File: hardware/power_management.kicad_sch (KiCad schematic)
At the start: 5 parts, among them Q1 IRLML6402, U2 BMS Module

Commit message: Added information, footprints and 3d models for several components
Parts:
- D3: Package (none) -> SOD-323F; Part Num (none) -> PMEG4010CEJ,115; Price/unit (none) -> $0.0699; Supplier Link (none) -> https://jlcpcb.com/partdetail/Nexperia-PMEG4010CEJ115/C50704
- Q1: Package (none) -> SOT-23; Part Num (none) -> IRLML6402TRPBF; Price/unit (none) -> $0.0906; Supplier Link (none) -> https://jlcpcb.com/partdetail/InfineonTechnologies-IRLML640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
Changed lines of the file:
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@@
 			)
 		)
-		(property "Datasheet" "https://assets.nexperia.com/documents/data-sheet/PMEG4010CEH_PMEG4010CEJ.pdf"
-			(at 177.8 74.93 0)
-			(effects
-				(font
-					(size 1.27 1.27)
-				)
-				(hide yes)
-			)
-		)
-		(property "Description" "40V, 1A very low Vf MEGA Schottky barrier rectifier, SOD-323F"
+		(property "Datasheet" "https://www.lcsc.com/datasheet/lcsc_datasheet_1809291616_Nexperia-PMEG4010CEJ-115_C50704.pdf"
+			(at 177.8 74.93 0)
+			(effects
+				(font
+					(size 1.27 1.27)
+				)
+				(hide yes)
+			)
+		)
+		(property "Description" "40V 570mV@1A 1A SOD-323F Schottky Diodes ROHS"
+			(at 177.8 74.93 0)
+			(effects
+				(font
+					(size 1.27 1.27)
+				)
+				(hide yes)
+			)
+		)
+		(property "Supplier Link" "https://jlcpcb.com/partdetail/Nexperia-PMEG4010CEJ115/C50704"
+			(at 177.8 74.93 0)
+			(effects
+				(font
+					(size 1.27 1.27)
+				)
+				(hide yes)
+			)
+		)
+		(property "Price/unit" "$0.0699"
+			(at 177.8 74.93 0)
+			(effects
+				(font
+					(size 1.27 1.27)
+				)
+				(hide yes)
+			)
+		)
+		(property "Part Num" "PMEG4010CEJ,115"
+			(at 177.8 74.93 0)
+			(effects
+				(font
+					(size 1.27 1.27)
+				)
+				(hide yes)
+			)
+		)
+		(property "Package" "SOD-323F"
 			(at 177.8 74.93 0)
 			(effects
@@
 			)
 		)
-		(property "Datasheet" "https://www.infineon.com/dgdl/irlml6402pbf.pdf?fileId=5546d462533600a401535668d5c2263c"
+		(property "Datasheet" "https://www.lcsc.com/datasheet/lcsc_datasheet_1810271032_Infineon-Technologies-IRLML6402TRPBF_C2593.pdf"
 			(at 173.99 93.98 0)
 			(effects
@@
 			)
 		)
-		(property "Description" "-3.7A Id, -20V Vds, 65mOhm Rds, P-Channel HEXFET Power MOSFET, SOT-23"
-			(at 170.18 88.9 0)
-			(effects
+		(property "Description" "20V 3.7A 1.3W 65mΩ@4.5V,3.7A 1.2V@250uA 1 Piece P-Channel SOT-23 MOSFETs ROHS"
+			(at 170.18 88.9 0)
+			(effects
+				(font
+					(size 1.27 1.27)
+				)
+				(hide yes)
+			)
+		)
+		(property "Supplier Link" "https://jlcpcb.com/partdetail/InfineonTechnologies-IRLML6402TRPBF/C2593"
+			(at 170.18 88.9 0)
+			(effects
+				(font
+					(size 1.27 1.27)
+				)
+				(hide yes)
+			)
+		)
+		(property "Price/unit" "$0.0906"
+			(at 170.18 88.9 0)
+			(effects
+				(font
+					(size 1.27 1.27)
+				)
+				(hide yes)
+			)
+		)
+		(property "Part Num" "IRLML6402TRPBF"
+			(at 170.18 88.9 0)
+			(effects
+				(font
+					(size 1.27 1.27)
+				)
+				(hide yes)
+			)
+		)
+		(property "Package" "SOT-23"
+			(at 170.18 88.9 0)
+			(effects

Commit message: Added some information to the microcontroller sch and the power_management sch
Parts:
- U2: Package (none) -> Module; Part Num (none) -> TP4056; Price/unit (none) -> 45 kr; Supplier Link (none) -> https://www.electrokit.com/batteriladdare-lipo-microusb
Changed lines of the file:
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@@
 			)
 		)
-		(property "Datasheet" ""
+		(property "Datasheet" "https://dlnmh9ip6v2uc.cloudfront.net/datasheets/Prototyping/TP4056.pdf"
 			(at 113.03 82.55 0)
 			(effects
@@
 			)
 		)
-		(property "Description" ""
+		(property "Description" "TP4056 laddare med skyddskrets för Li-Ion- och LiPo-cell"
 			(at 113.03 82.55 0)
 			(effects
 				(font
+					(size 1.27 1.27)
+				)
+				(hide yes)
+			)
+		)
+		(property "Package" "Module"
+			(at 113.03 81.28 0)
+			(effects
+				(font
+					(size 1.27 1.27)
+				)
+				(hide yes)
+			)
+		)
+		(property "Part Num" "TP4056"
+			(at 113.03 81.28 0)
+			(effects
+				(font
+					(size 1.27 1.27)
+				)
+				(hide yes)
+			)
+		)
+		(property "Price/unit" "45 kr"
+			(at 113.03 81.28 0)
+			(effects
+				(font
+					(size 1.27 1.27)
+				)
+				(hide yes)
+			)
+		)
+		(property "Supplier Link" "https://www.electrokit.com/batteriladdare-lipo-microusb"
+			(at 113.03 81.28 0)
+			(effects
+				(font

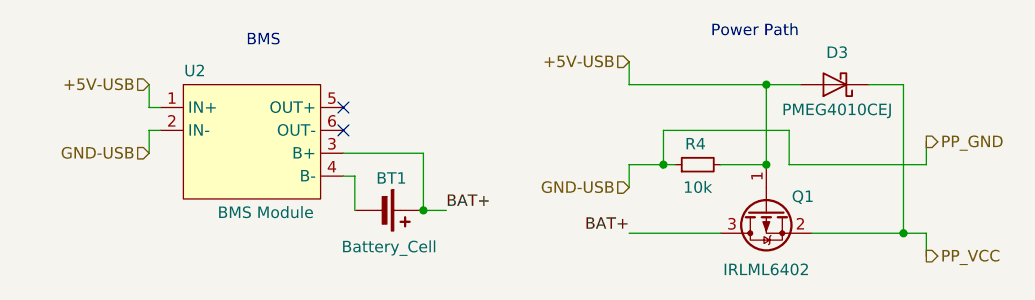
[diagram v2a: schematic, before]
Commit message: Added TP4056 footprint andconfirmed components in UART and BMS schematics.
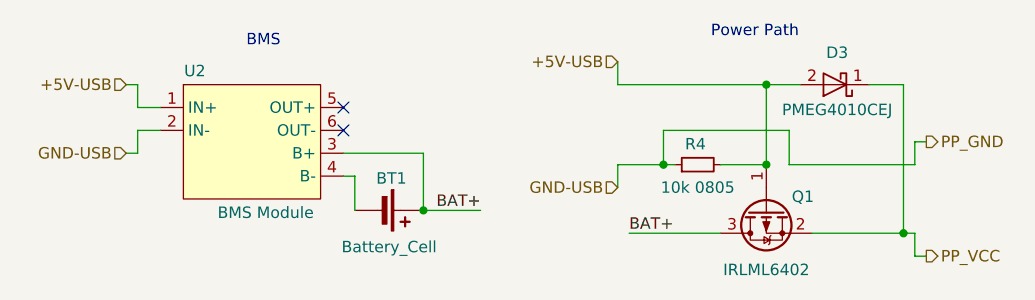
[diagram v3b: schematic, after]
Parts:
- R4: value 10k -> 10k 0805; Package (none) -> 0805; Part Num (none) -> 0805W8F1002T5E; Price/unit (none) -> $0.0017; Supplier Link (none) -> https://jlcpcb.com/partdetail/18102-0805W8F1002T5E/C17414
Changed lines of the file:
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@@
 	(wire
 		(pts
-			(xy 154.94 72.39) (xy 154.94 74.93)
-		)
-		(stroke
-			(width 0)
-			(type default)
-		)
-	)
-	(wire
-		(pts
-			(xy 185.42 91.44) (xy 187.96 91.44)
-		)
-		(stroke
-			(width 0)
-			(type default)
-		)
-	)
-	(wire
-		(pts
-			(xy 154.94 74.93) (xy 170.18 74.93)
+			(xy 186.69 81.28) (xy 187.96 81.28)
+		)
+		(stroke
+			(width 0)
+			(type default)
+		)
+	)
+	(wire
+		(pts
+			(xy 153.67 72.39) (xy 153.67 74.93)
+		)
+		(stroke
+			(width 0)
+			(type default)
+		)
+	)
+	(wire
+		(pts
+			(xy 185.42 91.44) (xy 186.69 91.44)
+		)
+		(stroke
+			(width 0)
+			(type default)
+		)
+	)
+	(wire
+		(pts
+			(xy 153.67 74.93) (xy 170.18 74.93)
 		)
 		(stroke
@@
 	(wire
 		(pts
-			(xy 132.08 88.9) (xy 134.62 88.9)
+			(xy 132.08 88.9) (xy 138.43 88.9)
+		)
+		(stroke
+			(width 0)
+			(type default)
+		)
+	)
+	(wire
+		(pts
+			(xy 100.33 74.93) (xy 100.33 77.47)
 		)
 		(stroke
@@
 	(wire
 		(pts
-			(xy 187.96 91.44) (xy 187.96 93.98)
+			(xy 186.69 91.44) (xy 186.69 93.98)
 		)
 		(stroke
@@
 	(wire
 		(pts
-			(xy 101.6 74.93) (xy 101.6 77.47)
-		)
-		(stroke
-			(width 0)
-			(type default)
-		)
-	)
-	(wire
-		(pts
-			(xy 154.94 83.82) (xy 158.75 83.82)
+			(xy 100.33 82.55) (xy 99.06 82.55)
+		)
+		(stroke
+			(width 0)
+			(type default)
+		)
+	)
+	(wire
+		(pts
+			(xy 153.67 83.82) (xy 158.75 83.82)
 		)
 		(stroke
@@
 	(wire
 		(pts
-			(xy 154.94 83.82) (xy 154.94 86.36)
-		)
-		(stroke
-			(width 0)
-			(type default)
-		)
-	)
-	(wire
-		(pts
-			(xy 101.6 77.47) (xy 102.87 77.47)
+			(xy 153.67 83.82) (xy 153.67 86.36)
+		)
+		(stroke
+			(width 0)
+			(type default)
+		)
+	)
+	(wire
+		(pts
+			(xy 100.33 77.47) (xy 102.87 77.47)
 		)
 		(stroke
@@
 	(wire
 		(pts
-			(xy 187.96 81.28) (xy 187.96 83.82)
+			(xy 186.69 81.28) (xy 186.69 83.82)
 		)
 		(stroke
@@
 	(wire
 		(pts
+			(xy 100.33 74.93) (xy 99.06 74.93)
+		)
+		(stroke
+			(width 0)
+			(type default)
+		)
+	)
+	(wire
+		(pts
 			(xy 123.19 82.55) (xy 132.08 82.55)
 		)
@@
 	(wire
 		(pts
-			(xy 187.96 83.82) (xy 172.72 83.82)
+			(xy 186.69 83.82) (xy 172.72 83.82)
 		)
 		(stroke
@@
 	(wire
 		(pts
+			(xy 100.33 80.01) (xy 100.33 82.55)
+		)
+		(stroke
+			(width 0)
+			(type default)
+		)
+	)
+	(wire
+		(pts
 			(xy 170.18 74.93) (xy 173.99 74.93)
 		)
@@
 	(wire
 		(pts
-			(xy 101.6 80.01) (xy 101.6 82.55)
+			(xy 186.69 93.98) (xy 187.96 93.98)
 		)
 		(stroke
@@
 	(wire
 		(pts
-			(xy 101.6 80.01) (xy 102.87 80.01)
+			(xy 100.33 80.01) (xy 102.87 80.01)
 		)
 		(stroke
@@
 	)
 	(label "BAT+"
-		(at 154.94 91.44 180)
+		(at 154.94 91.44 0)
+		(fields_autoplaced yes)
+		(effects
+			(font
+				(size 1.27 1.27)
+			)
+			(justify left bottom)
+		)
+	)
+	(label "BAT+"
+		(at 138.43 88.9 180)
 		(fields_autoplaced yes)
 		(effects
@@
 			)
 			(justify right bottom)
-		)
-	)
-	(label "BAT+"
-		(at 134.62 88.9 0)
-		(fields_autoplaced yes)
-		(effects
-			(font
-				(size 1.27 1.27)
-			)
-			(justify left bottom)
 		)
 	)
 	(hierarchical_label "GND-USB"
 		(shape input)
-		(at 154.94 86.36 180)
+		(at 153.67 86.36 180)
 		(fields_autoplaced yes)
 		(effects
@@
 	(hierarchical_label "+5V-USB"
 		(shape input)
-		(at 154.94 72.39 180)
+		(at 153.67 72.39 180)
 		(fields_autoplaced yes)
 		(effects
@@
 	(hierarchical_label "+5V-USB"
 		(shape input)
-		(at 101.6 74.93 180)
+		(at 99.06 74.93 180)
 		(fields_autoplaced yes)
 		(effects
@@
 	(hierarchical_label "GND-USB"
 		(shape input)
-		(at 101.6 82.55 180)
+		(at 99.06 82.55 180)
 		(fields_autoplaced yes)
 		(effects
@@
 			)
 		)
-		(property "Value" "10k"
+		(property "Value" "10k 0805"
 			(at 162.56 86.36 90)
 			(effects
@@
 			)
 		)
-		(property "Datasheet" "~"
-			(at 162.56 83.82 0)
-			(effects
-				(font
-					(size 1.27 1.27)
-				)
-				(hide yes)
-			)
-		)
-		(property "Description" "Resistor, small symbol"
-			(at 162.56 83.82 0)
-			(effects
+		(property "Datasheet" "https://jlcpcb.com/api/file/downloadByFileSystemAccessId/8562006748401074176"
+			(at 162.56 83.82 0)
+			(effects
+				(font
+					(size 1.27 1.27)
+				)
+				(hide yes)
+			)
+		)
+		(property "Description" "Resistor"
+			(at 162.56 83.82 0)
+			(effects
+				(font
+					(size 1.27 1.27)
+				)
+				(hide yes)
+			)
+		)
+		(property "Supplier Link" "https://jlcpcb.com/partdetail/18102-0805W8F1002T5E/C17414"
+			(at 162.56 83.82 0)
+			(effects
+				(font
+					(size 1.27 1.27)
+				)
+				(hide yes)
+			)
+		)
+		(property "Price/unit" "$0.0017"
+			(at 162.56 83.82 0)
+			(effects
+				(font
+					(size 1.27 1.27)
+				)
+				(hide yes)
+			)
+		)
+		(property "Part Num" "0805W8F1002T5E"
+			(at 162.56 83.82 0)
+			(effects
+				(font
+					(size 1.27 1.27)
+				)
+				(hide yes)
+			)
+		)
+		(property "Package" "0805"
+			(at 162.56 83.82 0)
+			(effects

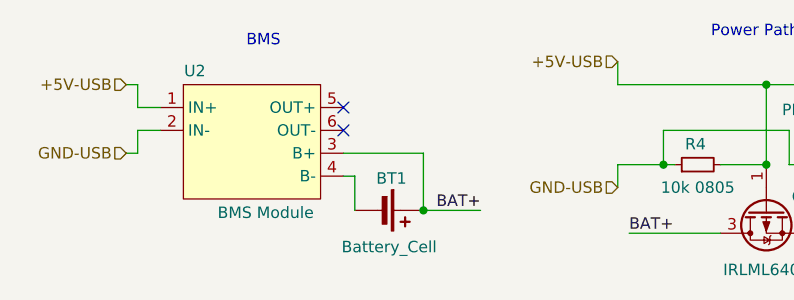
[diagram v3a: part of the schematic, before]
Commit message: Removed the 3.3V Regulator since we might need to run everything out of 5V
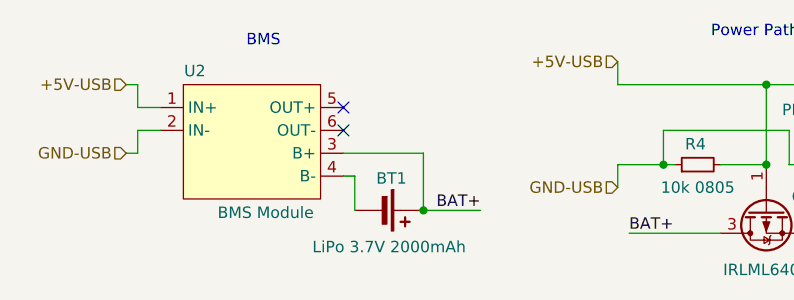
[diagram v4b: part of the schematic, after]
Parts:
- BT1: value Battery_Cell -> LiPo 3.7V 2000mAh
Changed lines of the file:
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@@
 			)
 		)
-		(property "Value" "Battery_Cell"
+		(property "Value" "LiPo 3.7V 2000mAh"
 			(at 128.27 92.964 90)
 			(effects
@@
 			(at 127 88.9 0)
 			(effects
+				(font
+					(size 1.27 1.27)
+				)
+				(hide yes)
+			)
+		)
+		(property "Supplier Link" ""
+			(at 127 88.9 0)
+			(effects
+				(font
+					(size 1.27 1.27)
+				)
+				(hide yes)
+			)
+		)
+		(property "Price/unit" ""
+			(at 127 88.9 0)
+			(effects
+				(font
+					(size 1.27 1.27)
+				)
+				(hide yes)
+			)
+		)
+		(property "Part Num" ""
+			(at 127 88.9 0)
+			(effects
+				(font
+					(size 1.27 1.27)
+				)
+				(hide yes)
+			)
+		)
+		(property "Package" ""
+			(at 127 88.9 0)
+			(effects

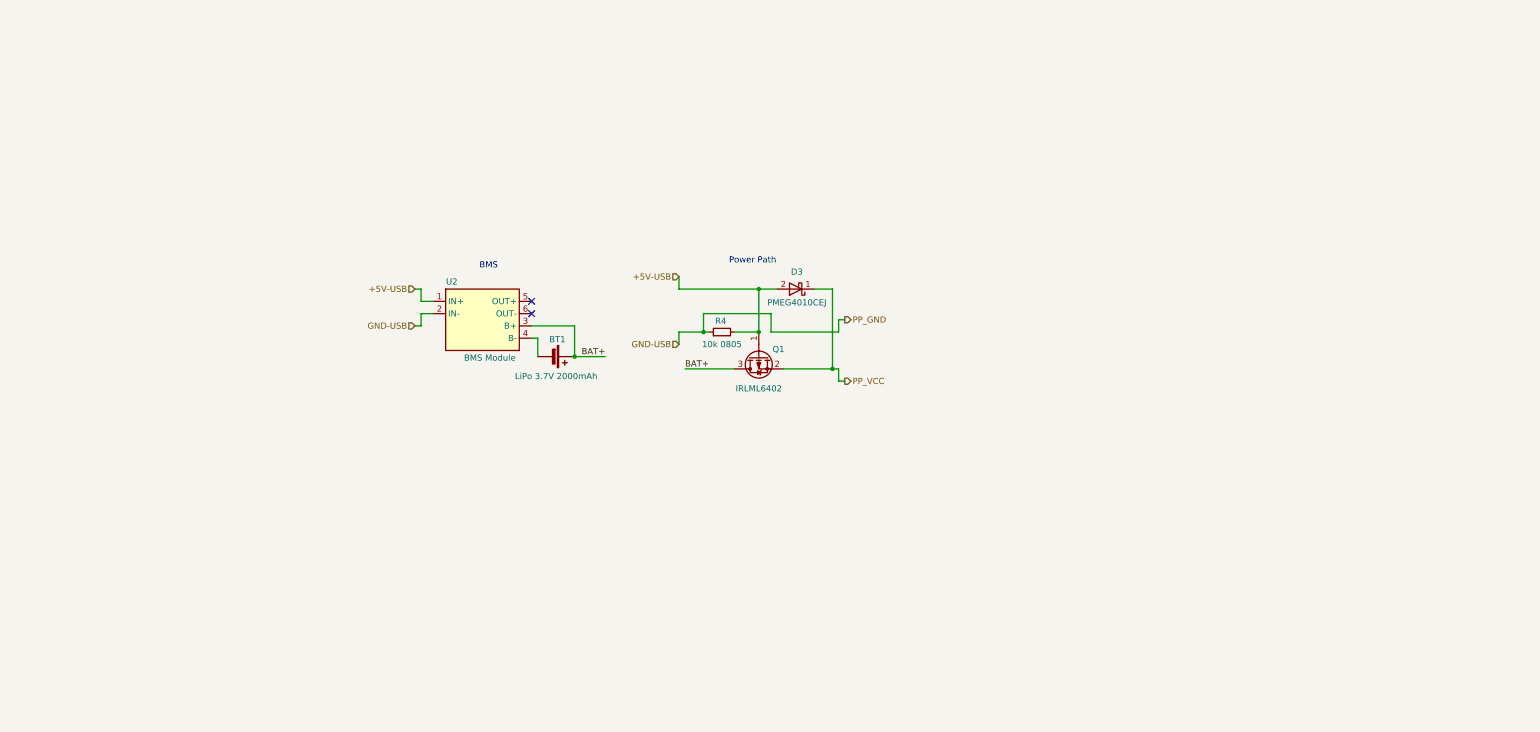
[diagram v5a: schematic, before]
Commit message: Schematic completed, commented and ready for review
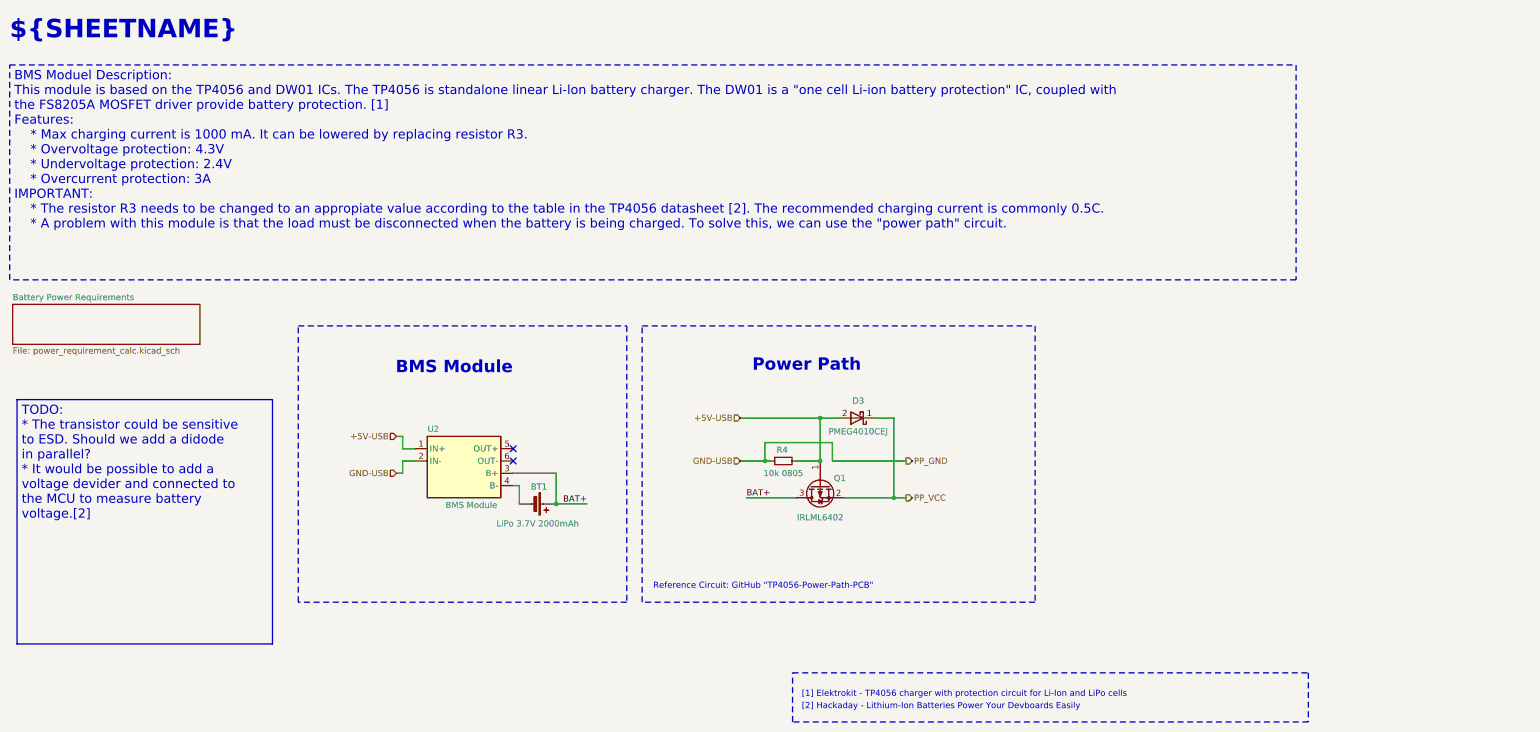
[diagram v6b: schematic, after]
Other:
- added sheet Battery Power Requirements (power_requirement_calc.kicad_sch)
- note added: "${SHEETNAME}"
- note added: "BMS Module"
- note added: "Reference Circuit: GitHub "TP4056-Power-Path-PCB""
- note added: "[1] Elektrokit - TP4056 charger with protection circuit for Li-Ion and LiPo cells"
- note added: "[2] Hackaday - Lithium-Ion Batteries Power Your Devboards Easily"
- note removed: "BMS"
- title: Kitchen_Timer - Power Management -> Kitchen_Timer - ${SHEETNAME}
- moved on the sheet: BT1, D3, Q1, R4, U2

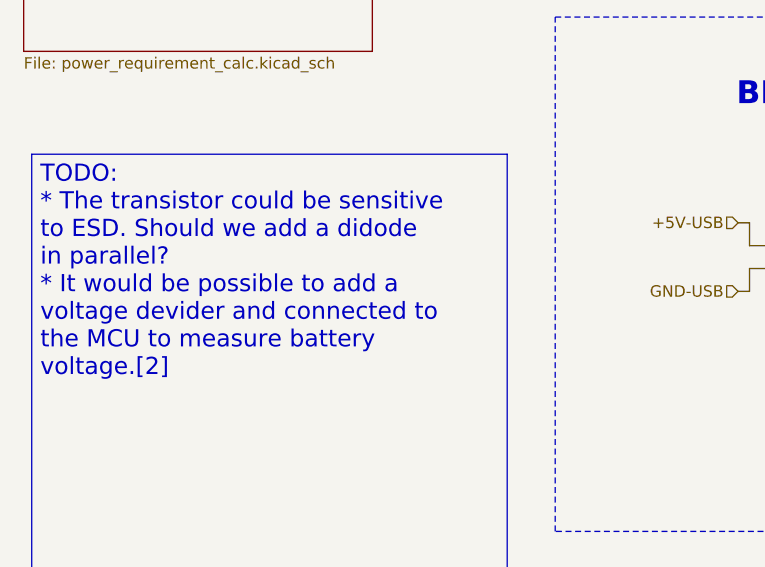
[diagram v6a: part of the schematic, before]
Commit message: Added comments to the TODO boxes after the meeting with Erasmus
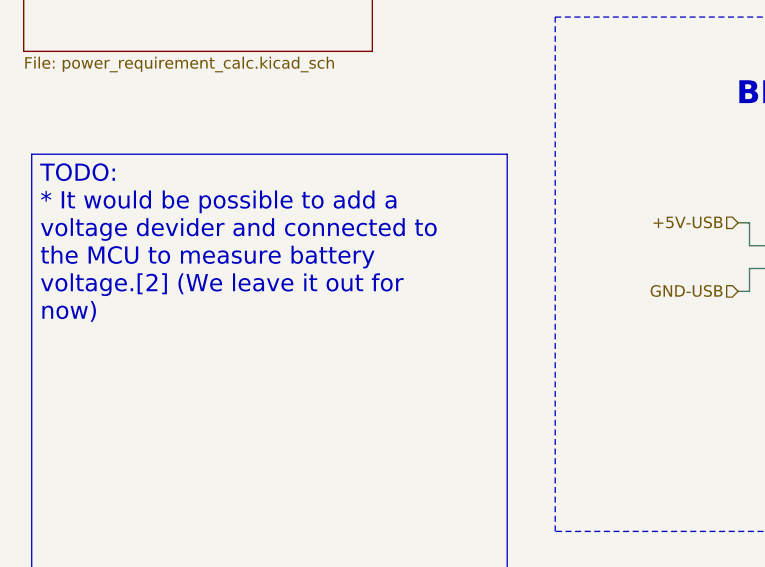
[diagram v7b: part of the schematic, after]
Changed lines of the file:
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@@
 		)
 	)
-	(text_box "TODO:\n* The transistor could be sensitive to ESD. Should we add a didode in parallel?\n* It would be possible to add a voltage devider and connected to the MCU to measure battery voltage.[2]\n"
+	(text_box "TODO:\n* It would be possible to add a voltage devider and connected to the MCU to measure battery voltage.[2] (We leave it out for now)\n"
 		(exclude_from_sim no)
 		(at 16.764 97.79 0)
